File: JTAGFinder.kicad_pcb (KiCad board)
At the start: 4 copper layers, 90 x 70 mm, 90 parts, among them J1 Conn_02x05_Odd_Even, J2 Conn_02x05_Odd_Even, J3 Conn_02x05_Odd_Even, J6 Bus_PCI_Express_x1_free_pins_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, P2 USB-TYPE-C-019, Q1 2N3904, SW1 SW_Push, U10 LFS0108, U11 SN74S1051, U12 SN74S1051, U13 P8X32A-Q44, U2 M24512E-FMN6TP, U3 MIC2025-2YM, U4 FT232RL, U5 TLV74033, U6 USBLC6-2SC6, U7 AD8655, U8 LFS0108, U9 LFS0108, Y1 5MHz

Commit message: [WIP] hw update
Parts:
- added H1: MH, MountingHole:MountingHole_3.5mm, F.Cu at (177.0, 124.0)
- added H2: MH, MountingHole:MountingHole_3.5mm, F.Cu at (177.0, 63.0)
- added H3: MH, MountingHole:MountingHole_3.5mm, F.Cu at (109.0, 63.0)
- added H4: MH, MountingHole:MountingHole_3.5mm, F.Cu at (109.0, 124.0)
- moved C20 62.1 mm to (158.4, 124.0), turned to -90 degrees
- moved C23 56.6 mm to (161.0, 124.0), turned to -90 degrees
- moved R21 54.6 mm to (172.6, 119.5), turned to 0 degrees
- moved R17 50.8 mm to (177.1, 110.0), turned to 0 degrees
- moved R29 50.3 mm to (177.2, 100.6), turned to 0 degrees
- moved R19 50.0 mm to (177.1, 114.7), turned to 0 degrees
- moved R25 49.5 mm to (177.1, 93.6), turned to 0 degrees
- moved R27 49.5 mm to (177.1, 96.0), turned to 0 degrees
- moved R22 40.4 mm to (170.9, 122.1)
- moved C24 39.4 mm to (161.0, 111.0), turned to -90 degrees
- moved R15 39.0 mm to (177.2, 105.3)
- moved J1 37.5 mm to (186.0, 109.0), turned to 0 degrees
- moved R16 36.8 mm to (177.1, 107.6)
- moved J2 36.7 mm to (186.0, 87.0), turned to 0 degrees
- moved R23 36.2 mm to (177.1, 86.7)
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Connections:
- U11 pad 10: CH06 -> CH11
- U11 pad 11: CH07 -> CH10
- U11 pad 12: CH11 -> CH09
- U11 pad 13: CH10 -> CH08
- U11 pad 14: CH09 -> CH07
- U11 pad 15: CH08 -> CH06
- U11 pad 2: CH00 -> CH05
- U11 pad 3: CH01 -> CH04
- U11 pad 4: CH02 -> CH03
- U11 pad 5: CH03 -> CH02
- U11 pad 6: CH04 -> CH01
- U11 pad 7: CH05 -> CH00
- U12 pad 10: CH23 -> CH16
- U12 pad 11: CH22 -> CH17
- U12 pad 12: CH21 -> CH18
- U12 pad 13: CH20 -> CH19
- U12 pad 14: CH19 -> CH20
- U12 pad 15: CH18 -> CH21
- U12 pad 2: CH12 -> CH15
- U12 pad 3: CH13 -> CH14
- U12 pad 4: CH14 -> CH13
- U12 pad 5: CH15 -> CH12
- U12 pad 6: CH16 -> CH23
- U12 pad 7: CH17 -> CH22
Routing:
- net TXSOE: track 0.00 -> 69.0 mm, vias 0 -> 4
- net P7: track 28.5 -> 82.6 mm
- net P18: track 55.0 -> 98.2 mm, vias 0 -> 1
- net P21: track 62.9 -> 105.6 mm, vias 0 -> 1
- net P17: track 55.1 -> 97.5 mm, vias 0 -> 1
- net P19: track 58.8 -> 101.1 mm, vias 0 -> 1
- net P16: track 64.9 -> 106.7 mm, vias 0 -> 1
- net P22: track 57.4 -> 98.0 mm, vias 0 -> 1
- net CH19: track 0.00 -> 39.8 mm, vias 0 -> 1
- net P20: track 56.5 -> 95.9 mm, vias 0 -> 1
- net CH20: track 0.00 -> 37.8 mm, vias 0 -> 2
- net CH21: track 0.00 -> 36.6 mm
- net CH22: track 0.00 -> 34.5 mm, vias 0 -> 3
- net CH07: track 0.00 -> 31.4 mm, vias 0 -> 2
- net CH06: track 0.00 -> 29.2 mm, vias 0 -> 2
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- added copper zone on In4.Cu, net GND
- added copper zone on In3.Cu, net Vdrive
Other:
- copper layers 4 -> 6

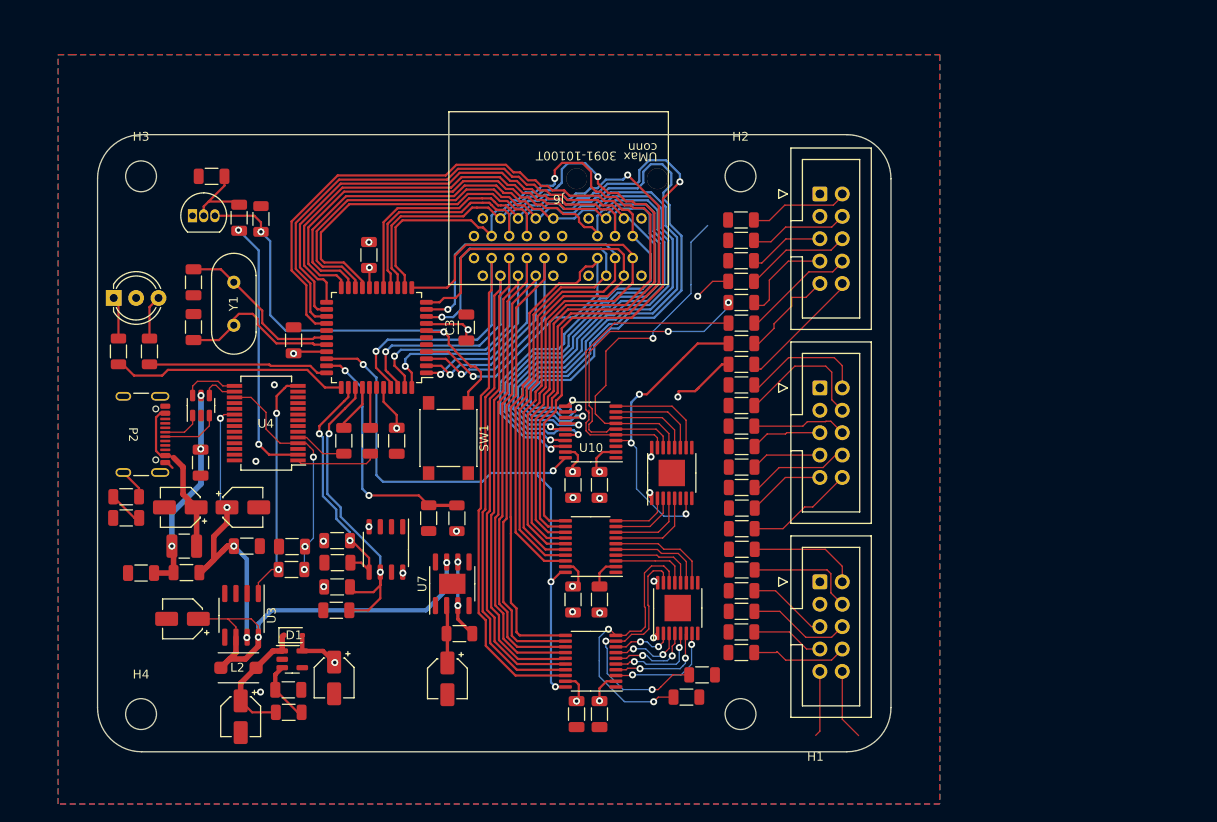
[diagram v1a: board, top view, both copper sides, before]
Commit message: text labels and route finished
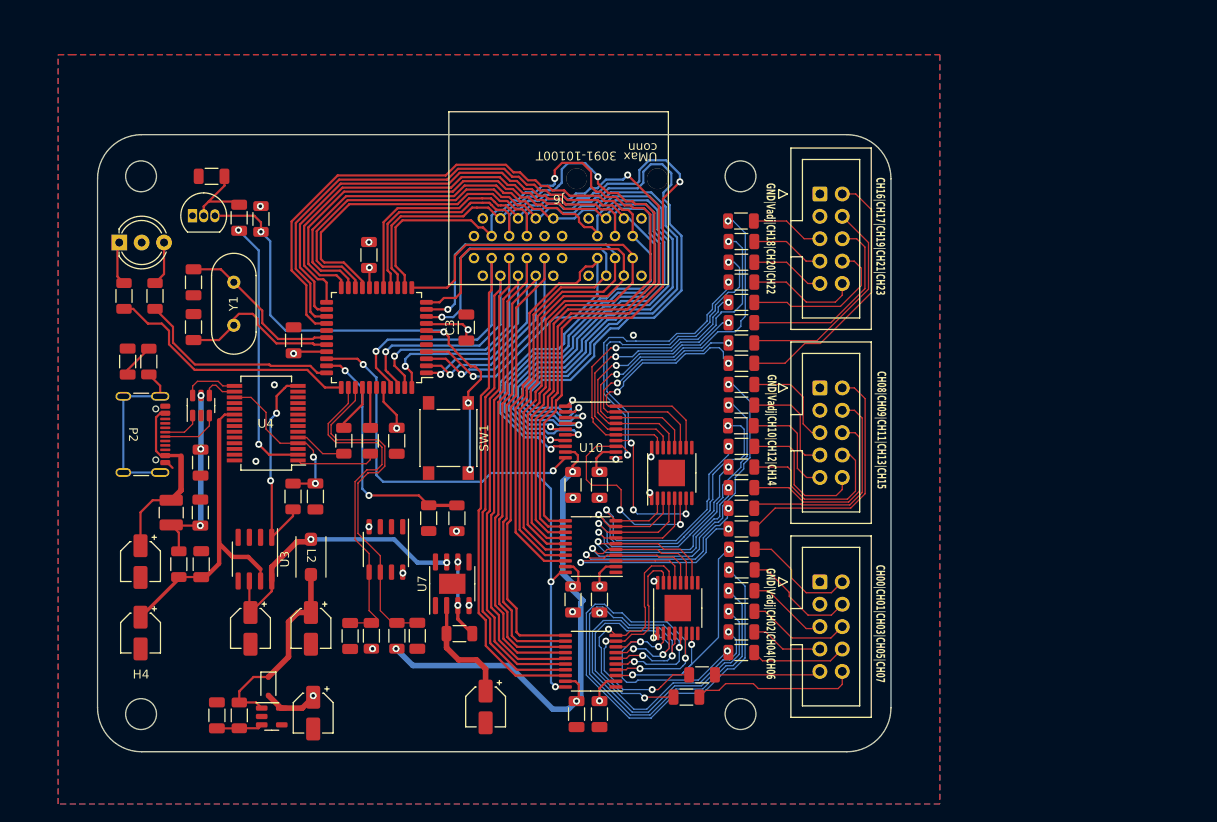
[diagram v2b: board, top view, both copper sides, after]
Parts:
- moved C6 18.4 mm to (108.9, 114.8), turned to -90 degrees
- moved C19 17.7 mm to (107.5, 84.0), turned to 90 degrees
- moved R23 16.3 mm to (177.1, 103.0)
- moved R14 15.6 mm to (109.9, 84.0), turned to 90 degrees
- moved L2 15.0 mm to (128.3, 106.2), turned to -90 degrees
- moved C12 12.8 mm to (128.3, 114.3)
- moved R24 11.7 mm to (177.1, 100.7)
- moved R34 11.7 mm to (177.1, 79.6)
- moved R3 11.5 mm to (135.1, 115.1), turned to 90 degrees
- moved C5 9.63 mm to (140.3, 115.1), turned to -90 degrees
- moved C8 9.60 mm to (115.7, 101.1), turned to 90 degrees
- moved R29 9.34 mm to (177.0, 91.3)
- moved R30 9.34 mm to (177.1, 93.6)
- moved R32 9.33 mm to (177.1, 81.9)
- moved R38 9.33 mm to (177.1, 75.0)
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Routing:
- net CH01: track 11.7 -> 67.7 mm, vias 2 -> 3
- net +3.3V: track 35.3 -> 86.9 mm, vias 11 -> 12
- net CH23: track 7.92 -> 58.4 mm, vias 1 -> 4
- net CH02: track 10.8 -> 60.5 mm, vias 2 -> 3
- net CH03: track 9.67 -> 53.2 mm, vias 2 -> 3
- net CH04: track 8.64 -> 47.6 mm, vias 2 -> 3
- net CH10: track 11.0 -> 49.5 mm, vias 0 -> 2
- net CH18: track 9.24 -> 46.2 mm, vias 0 -> 2
- net CH12: track 10.4 -> 44.4 mm, vias 0 -> 2
- net CH14: track 7.68 -> 40.3 mm, vias 0 -> 2
- net CH15: track 6.71 -> 32.2 mm, vias 0 -> 2
- net CH13: track 9.16 -> 33.7 mm, vias 0 -> 2
- net CH09: track 9.86 -> 33.7 mm, vias 0 -> 2
- net CH08: track 8.83 -> 32.1 mm, vias 0 -> 2
- net CH11: track 11.9 -> 34.7 mm, vias 0 -> 2
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- added copper zone on In2.Cu, net Vdrive
- removed copper zone on In4.Cu, net GND
- removed copper zone on In3.Cu, net Vdrive
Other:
- copper layers 6 -> 4
- board text added: "CH00|CH01|CH03|CH05|CH07"
- board text added: "CH08|CH09|CH11|CH13|CH15"
- board text added: "CH16|CH17|CH19|CH21|CH23"
- board text added: "GND|Vadj|CH02|CH04|CH06"
- board text added: "GND|Vadj|CH10|CH12|CH14"
- board text added: "GND|Vadj|CH18|CH20|CH22"

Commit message: finished rev1
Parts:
- removed P2: USB-TYPE-C-019, Connector_USB:USB_C_Receptacle_GCT_USB4105-xx-A_16P_TopMnt_Horizontal
- added J4: USB_C_Receptacle_USB2.0, Connector_USB:USB_C_Receptacle_HRO_TYPE-C-31-M-12, F.Cu at (108.0, 92.2)
- moved C12 11.6 mm to (134.8, 124.0)
- moved R9 9.66 mm to (148.8, 123.8), turned to -90 degrees
- moved C9 8.96 mm to (127.9, 108.2)
- moved R5 8.96 mm to (125.4, 108.2)
- moved R11 8.27 mm to (142.5, 110.0), turned to -90 degrees
- moved R10 8.21 mm to (145.0, 110.0)
- moved L2 7.97 mm to (126.8, 114.0)
- moved C11 7.63 mm to (113.8, 114.8)
- moved U7 7.16 mm to (144.1, 116.4)
- moved U3 6.61 mm to (121.2, 113.0)
- moved C16 4.40 mm to (143.8, 124.0)
- moved U2 2.48 mm to (136.4, 107.8)
- moved C4 1.86 mm to (131.2, 114.0)
- moved C5 1.86 mm to (138.9, 114.0)
- moved R4 1.86 mm to (136.6, 114.0)
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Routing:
- net DACOUT: track 28.0 -> 39.1 mm
- net ~EN_MIC2025: track 23.4 -> 34.4 mm
- net /USB_input_interface/VCC_IO: track 18.9 -> 29.4 mm, vias 2 -> 0
- net VDD: track 21.5 -> 29.0 mm
- net +5V: track 32.3 -> 39.5 mm
- net /USB_input_interface/USBN: track 6.67 -> 13.3 mm, vias 0 -> 2
- net Vdrive: track 27.2 -> 21.2 mm, vias 10 -> 11
- net +3.3V: track 86.9 -> 92.3 mm, vias 12 -> 11
- net /USB_input_interface/USBP: track 4.45 -> 9.05 mm, vias 0 -> 2
- net VCC: track 37.3 -> 41.3 mm
- net Net-(U7--): track 12.8 -> 9.76 mm
- net Net-(D1-K): track 22.5 -> 25.5 mm
- net GND: track 1.25 -> 3.90 mm
- net TXSOE: track 69.0 -> 71.1 mm, vias 4 -> 3
- net CH08: track 32.1 -> 30.1 mm
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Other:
- board text added: "@fmawic"
- board text added: "HW v1.0"
- board text added: "I2C Flash"
- board text added: "JTAG Finder"
- board text added: "Level Shifters"
- board text added: "Protections ESD"
- board text added: "RESET"
- board text added: "Supply +3.3V"
- board text added: "Supply +5 V @500 mA"
- board text added: "Vadj 0~3.3 V"
- board text added: "steps ~ 25mV @300mA"

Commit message: finish update extra updates
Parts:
- removed R34, R35, R36, R37, R38: 1k, Resistor_SMD:R_1206_3216Metric
- removed U10: LFS0108, Package_SO:TSSOP-20_4.4x6.5mm_P0.65mm
- added J10: V_drive, Connector_PinHeader_2.54mm:PinHeader_1x05_P2.54mm_Vertical, F.Cu at (188.2, 68.4)
- added J5: BT_HC08_SERIAL_COM, Connector_PinHeader_2.54mm:PinHeader_1x04_P2.54mm_Vertical, F.Cu at (138.2, 100.8)
- added J7: GND, Connector_PinHeader_2.54mm:PinHeader_1x05_P2.54mm_Vertical, F.Cu at (192.0, 68.4)
- added J8: GPIO_19-23, Connector_PinHeader_2.54mm:PinHeader_1x05_P2.54mm_Vertical, F.Cu at (180.8, 68.4)
- added J9: +3V3, Connector_PinHeader_2.54mm:PinHeader_1x05_P2.54mm_Vertical, F.Cu at (184.5, 68.4)
- added R39: 10k, Resistor_SMD:R_1206_3216Metric, F.Cu at (107.0, 99.2)
- added R40: 10k, Resistor_SMD:R_1206_3216Metric, F.Cu at (107.0, 101.8)
- J3: value Conn_02x05_Odd_Even -> LCD_IIC; footprint Connector_IDC:IDC-Header_2x05_P2.54mm_Vertical -> Connector_PinHeader_2.54mm:PinHeader_1x04_P2.54mm_Vertical
- R31, R32, R33: value 1k -> 10k
- SW1: footprint Button_Switch_SMD:SW_SPST_PTS645 -> Button_Switch_SMD:SW_SPST_CK_KXT3
- moved J3 69.8 mm to (126.2, 101.0), turned to 90 degrees
- moved R31 15.6 mm to (172.8, 69.2), turned to -90 degrees
- moved R32 12.8 mm to (175.2, 69.2), turned to -90 degrees
- moved R33 6.85 mm to (170.3, 69.2), turned to -90 degrees
- moved SW1 4.07 mm to (143.1, 88.2), turned to 180 degrees
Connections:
- J3 pad 2: /Protected Output/C16 -> +3.3V
- J3 pad 3: Vdrive -> SCL
- J3 pad 4: /Protected Output/C17 -> SDA
- J4 pad A5: unconnected-(J4-CC1-PadA5) -> /USB_input_interface/cc1
- J4 pad B5: unconnected-(J4-CC2-PadB5) -> /USB_input_interface/cc2
- R31 pad 1: CH16 -> P16
- R31 pad 2: /Protected Output/C16 -> GND
- R32 pad 1: CH17 -> P17
- R32 pad 2: /Protected Output/C17 -> GND
- R33 pad 1: CH18 -> P18
- R33 pad 2: /Protected Output/C18 -> GND
- U12 pad 10: CH16 -> unconnected-(U12-D07-Pad10)
- U12 pad 11: CH17 -> unconnected-(U12-D08-Pad11)
- U12 pad 12: CH18 -> unconnected-(U12-D09-Pad12)
- U12 pad 13: CH19 -> unconnected-(U12-D10-Pad13)
- U12 pad 14: CH20 -> unconnected-(U12-D11-Pad14)
- U12 pad 15: CH21 -> unconnected-(U12-D12-Pad15)
- U12 pad 6: CH23 -> unconnected-(U12-D05-Pad6)
- U12 pad 7: CH22 -> unconnected-(U12-D06-Pad7)
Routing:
- net CH23: track 58.4 -> 0.00 mm, vias 4 -> 0
- net CH22: track 52.9 -> 0.00 mm, vias 4 -> 0
- net CH18: track 46.2 -> 0.00 mm, vias 2 -> 0
- net P16: track 106.7 -> 62.8 mm
- net CH20: track 43.6 -> 0.00 mm, vias 2 -> 0
- net P18: track 98.2 -> 58.1 mm
- net +3.3V: track 92.3 -> 132.1 mm, vias 11 -> 13
- net CH21: track 34.8 -> 0.00 mm, vias 2 -> 0
- net P17: track 97.5 -> 62.8 mm
- net CH19: track 31.9 -> 0.00 mm, vias 2 -> 0
- net CH16: track 31.4 -> 0.00 mm, vias 2 -> 0
- net CH17: track 30.5 -> 0.00 mm, vias 2 -> 0
- net /Protected Output/C16: track 30.1 -> 0.00 mm
- net P21: track 105.6 -> 75.8 mm, vias 1 -> 0
- net P19: track 101.1 -> 72.8 mm, vias 1 -> 0
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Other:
- board text added: "+3.3 V"
- board text added: "3.3V|GND|TXD|RXD"
- board text added: "BT_Module (HC08)"
- board text added: "GND"
- board text added: "GND|3.3V|SCL|SDA"
- board text added: "HW v1.1"
- board text added: "P19|P20|P21|P22|P23"
- board text added: "V_drive"
- board text removed: "CH16|CH17|CH19|CH21|CH23"
- board text removed: "GND|Vadj|CH18|CH20|CH22"
- board text removed: "HW v1.0"

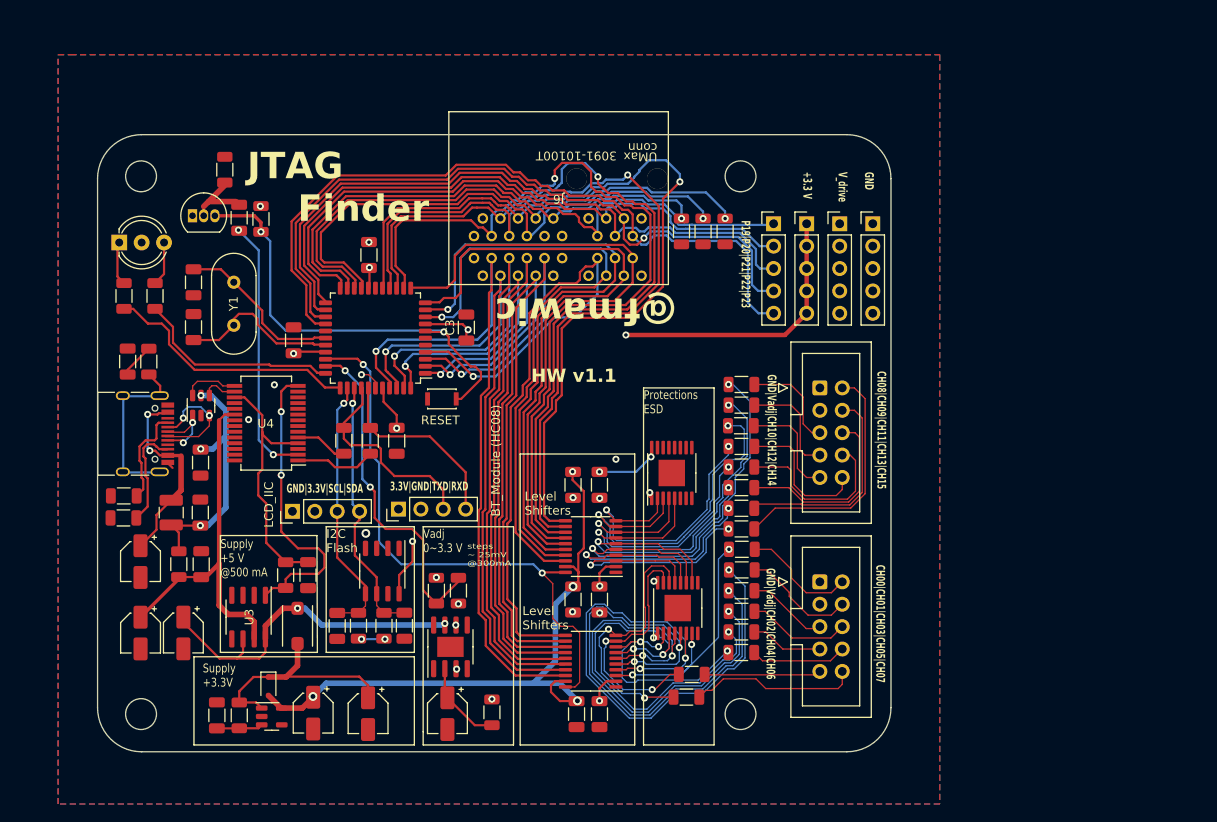
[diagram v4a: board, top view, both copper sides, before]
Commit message: finished two layer version
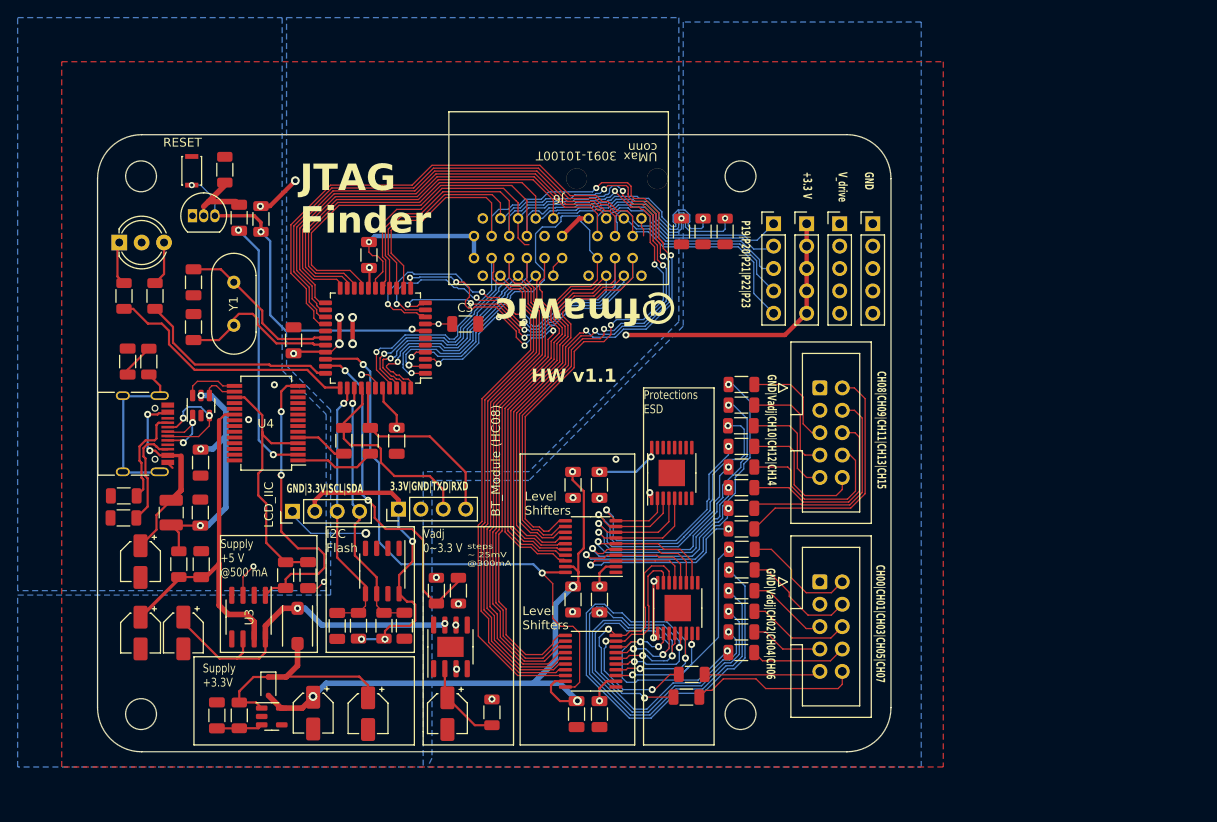
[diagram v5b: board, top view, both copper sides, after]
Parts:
- moved SW1 38.4 mm to (114.8, 62.4), turned to 90 degrees
- moved C3 0.42 mm to (145.8, 79.8), turned to 0 degrees
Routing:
- net +3.3V: track 132.1 -> 173.9 mm, vias 13 -> 18
- net GND: track 3.90 -> 42.7 mm, vias 11 -> 13
- net P7: track 82.9 -> 97.8 mm
- net P9: track 73.1 -> 84.4 mm, vias 1 -> 3
- net P8: track 72.4 -> 82.4 mm, vias 1 -> 3
- net /uController/ ~RES: track 50.2 -> 40.2 mm, vias 2 -> 3
- net P16: track 62.8 -> 72.2 mm
- net P11: track 73.2 -> 82.5 mm, vias 0 -> 3
- net P12: track 95.4 -> 103.9 mm, vias 1 -> 3
- net P17: track 62.8 -> 70.9 mm
- net P4: track 74.0 -> 81.6 mm
- net Vdrive: track 17.0 -> 23.4 mm
- net P5: track 70.5 -> 76.5 mm
- net P3: track 74.6 -> 80.0 mm
- net P14: track 96.0 -> 100.7 mm, vias 1 -> 3
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- added copper zone on B.Cu, net (none)
- added copper zone on B.Cu, net +3.3V
- added copper zone on B.Cu, net Vdrive
- removed copper zone on In2.Cu, net +3.3V
- removed copper zone on B.Cu, net GND
- removed copper zone on In1.Cu, net GND
- removed copper zone on In2.Cu, net Vdrive
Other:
- copper layers 4 -> 2
